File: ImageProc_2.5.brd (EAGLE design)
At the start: 49.8 x 23.2 mm, 117 parts, among them IC1 XC61GC3002HR-G, IC10 AT45DB642D-CNU, IC2 MIC5335-SPYMT, IC3 MIC5335-JGYMT, IC4 DSPIC33FJ128MC706A, IC5 AT86RF233-ZU, IC6 LTC6088, IC7 DRV8833RTY, IC8 DRV8833RTY, IC9 MPU-6000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

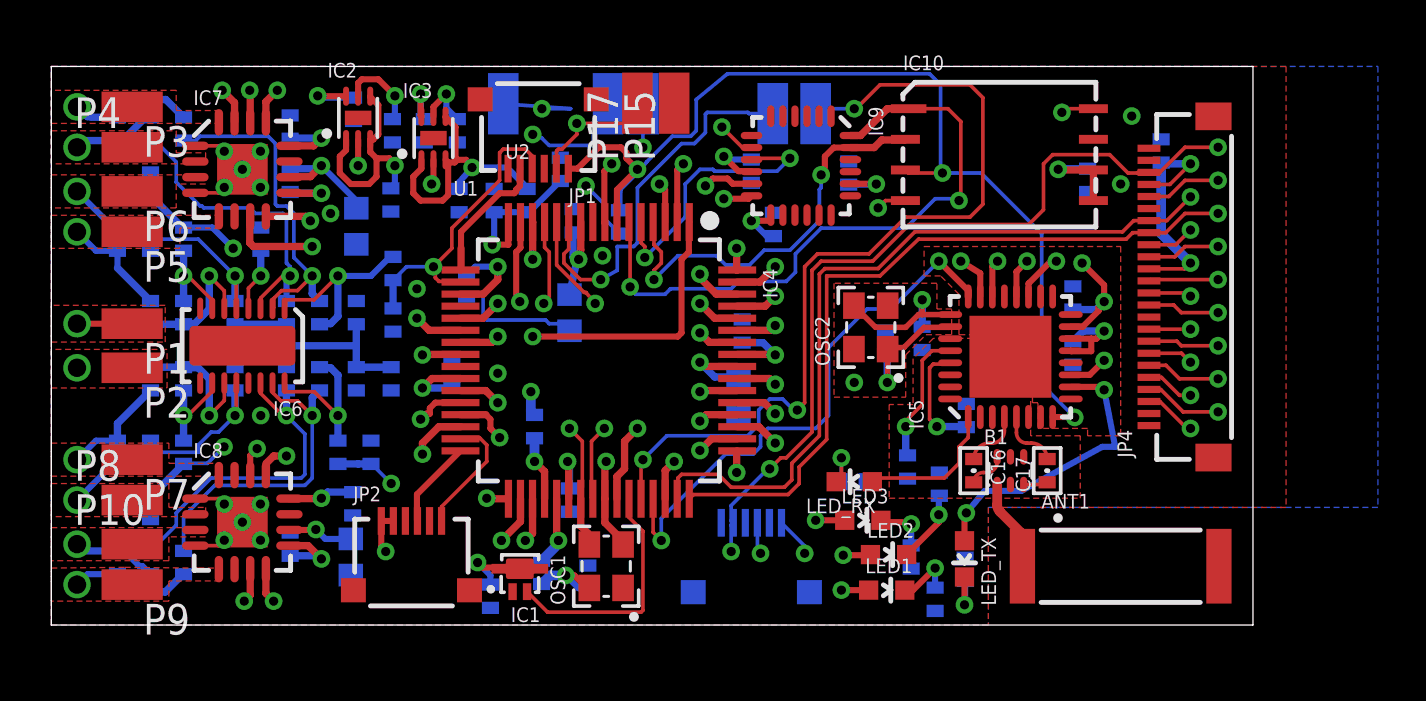
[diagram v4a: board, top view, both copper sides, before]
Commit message: Zero Airwires, fixed the restrict DRC errors.
Now proceeding to (hopefully final) DRC
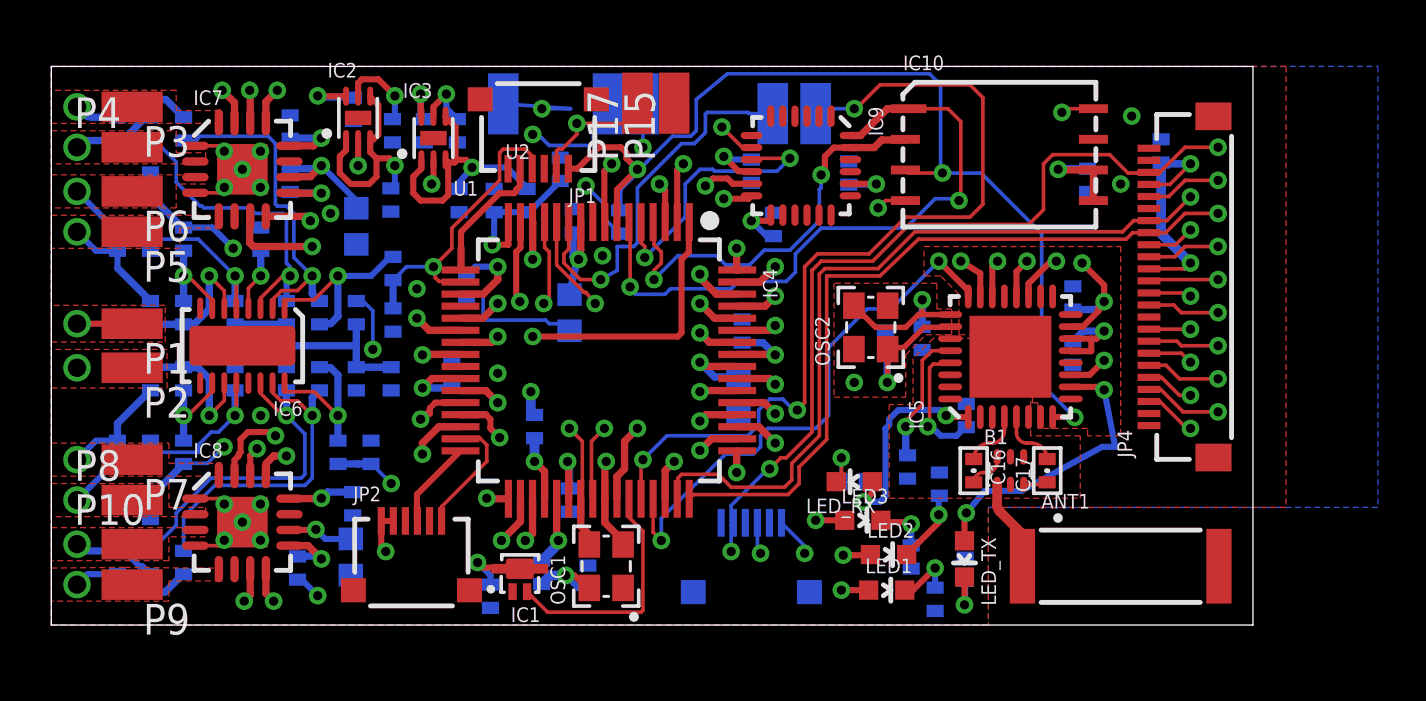
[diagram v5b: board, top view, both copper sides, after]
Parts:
- moved C34 1.04 mm to (10.2, 2.36), turned to 90 degrees
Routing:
- net V_BATT: track 37.6 -> 41.9 mm, vias 8 -> 10
- net N$13: track 5.99 -> 9.04 mm, vias 0 -> 2
- net 3.3V: track 61.2 -> 63.6 mm, vias 16 -> 17
- net N$3: track 4.73 -> 5.31 mm
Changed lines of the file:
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@@
 <grid distance="3" unitdist="mil" unit="mil" style="lines" multiple="1" display="yes" altdistance="1" altunitdist="mil" altunit="mil"/>
 <layers>
-<layer number="1" name="Top" color="4" fill="1" visible="no" active="yes"/>
+<layer number="1" name="Top" color="4" fill="1" visible="yes" active="yes"/>
 <layer number="2" name="Ground" color="2" fill="1" visible="no" active="yes"/>
 <layer number="3" name="Power" color="5" fill="1" visible="no" active="yes"/>
@@
 <layer number="14" name="Route14" color="1" fill="6" visible="no" active="no"/>
 <layer number="15" name="Route15" color="4" fill="6" visible="no" active="no"/>
-<layer number="16" name="Bottom" color="1" fill="1" visible="yes" active="yes"/>
+<layer number="16" name="Bottom" color="1" fill="1" visible="no" active="yes"/>
 <layer number="17" name="Pads" color="2" fill="1" visible="no" active="yes"/>
 <layer number="18" name="Vias" color="2" fill="1" visible="yes" active="yes"/>
-<layer number="19" name="Unrouted" color="6" fill="1" visible="yes" active="yes"/>
+<layer number="19" name="Unrouted" color="6" fill="1" visible="no" active="yes"/>
 <layer number="20" name="Dimension" color="15" fill="1" visible="no" active="yes"/>
 <layer number="21" name="tPlace" color="16" fill="1" visible="no" active="yes"/>
 <layer number="22" name="bPlace" color="14" fill="1" visible="no" active="yes"/>
 <layer number="23" name="tOrigins" color="15" fill="1" visible="no" active="yes"/>
-<layer number="24" name="bOrigins" color="15" fill="1" visible="no" active="yes"/>
+<layer number="24" name="bOrigins" color="15" fill="1" visible="yes" active="yes"/>
 <layer number="25" name="tNames" color="7" fill="1" visible="no" active="yes"/>
 <layer number="26" name="bNames" color="7" fill="1" visible="no" active="yes"/>
@@
 <layer number="39" name="tKeepout" color="4" fill="11" visible="no" active="yes"/>
 <layer number="40" name="bKeepout" color="1" fill="11" visible="no" active="yes"/>
-<layer number="41" name="tRestrict" color="4" fill="10" visible="no" active="yes"/>
-<layer number="42" name="bRestrict" color="1" fill="10" visible="no" active="yes"/>
+<layer number="41" name="tRestrict" color="4" fill="10" visible="yes" active="yes"/>
+<layer number="42" name="bRestrict" color="1" fill="10" visible="yes" active="yes"/>
 <layer number="43" name="vRestrict" color="2" fill="10" visible="no" active="yes"/>
 <layer number="44" name="Drills" color="7" fill="1" visible="no" active="yes"/>
@@
 <attribute name="TECHNOLOGY" value="CERAMIC" x="9.906" y="18.4404" size="1.778" layer="28" rot="MR270" display="off"/>
 </element>
-<element name="C34" library="biomimetic" package="0402-CAP" value="10nF" x="9.906" y="3.3528" locked="yes" rot="MR270">
-<attribute name="AUTHOR" value="Ryan Julian (ryanjulian@berkeley.edu)" x="9.906" y="3.3528" size="1.778" layer="28" rot="MR270" display="off"/>
-<attribute name="REVISION" value="1" x="9.906" y="3.3528" size="1.778" layer="28" rot="MR270" display="off"/>
-<attribute name="YEAR" value="2012" x="9.906" y="3.3528" size="1.778" layer="28" rot="MR270" display="off"/>
-<attribute name="DIELECTRIC" value="X7R" x="9.906" y="3.3528" size="1.778" layer="28" rot="MR270" display="off"/>
-<attribute name="TECHNOLOGY" value="CERAMIC" x="9.906" y="3.3528" size="1.778" layer="28" rot="MR270" display="off"/>
-<attribute name="VOLTAGE" value="16V" x="9.906" y="3.3528" size="1.778" layer="28" rot="MR270" display="off"/>
+<element name="C34" library="biomimetic" package="0402-CAP" value="10nF" x="10.2108" y="2.3622" rot="MR90">
+<attribute name="AUTHOR" value="Ryan Julian (ryanjulian@berkeley.edu)" x="10.2108" y="2.3622" size="1.778" layer="28" rot="MR90" display="off"/>
+<attribute name="REVISION" value="1" x="10.2108" y="2.3622" size="1.778" layer="28" rot="MR90" display="off"/>
+<attribute name="YEAR" value="2012" x="10.2108" y="2.3622" size="1.778" layer="28" rot="MR90" display="off"/>
+<attribute name="DIELECTRIC" value="X7R" x="10.2108" y="2.3622" size="1.778" layer="28" rot="MR90" display="off"/>
+<attribute name="TECHNOLOGY" value="CERAMIC" x="10.2108" y="2.3622" size="1.778" layer="28" rot="MR90" display="off"/>
+<attribute name="VOLTAGE" value="16V" x="10.2108" y="2.3622" size="1.778" layer="28" rot="MR90" display="off"/>
 </element>
 <element name="C24" library="biomimetic" package="0402-CAP" value="0.1uF" x="2.7432" y="20.574" rot="MR270">
@@
 <wire x1="30.2822" y1="4.2396" x2="31.242" y2="3.2798" width="0.1524" layer="16"/>
 <wire x1="31.242" y1="3.2798" x2="31.242" y2="2.9718" width="0.1524" layer="16"/>
-<wire x1="8.6868" y1="14.478" x2="12.6492" y2="13.4366" width="0" layer="19" extent="1-16"/>
+<via x="13.335" y="11.43" extent="1-16" drill="0.381"/>
+<wire x1="13.335" y1="11.43" x2="13.335" y2="13.0302" width="0.1524" layer="16"/>
+<wire x1="13.335" y1="13.0302" x2="12.9286" y2="13.4366" width="0.1524" layer="16"/>
+<wire x1="12.9286" y1="13.4366" x2="12.6492" y2="13.4366" width="0.1524" layer="16"/>
 </signal>
 <signal name="N$6">
@@
 <contactref element="IC5" pad="1"/>
 <wire x1="34.0494" y1="5.9436" x2="34.2018" y2="6.096" width="0.1524" layer="1"/>
-<wire x1="34.2018" y1="6.096" x2="37.0332" y2="6.096" width="0.1524" layer="1"/>
-<wire x1="37.0332" y1="6.096" x2="37.6428" y2="6.7056" width="0.1524" layer="1"/>
-<wire x1="37.6428" y1="6.7056" x2="37.6428" y2="7.3914" width="0.1524" layer="1"/>
-<wire x1="37.6428" y1="7.3914" x2="38.0264" y2="7.775" width="0.1524" layer="1"/>
-<wire x1="38.0264" y1="7.775" x2="38.0264" y2="8.6252" width="0.1524" layer="1"/>
+<via x="33.6804" y="5.1054" extent="1-16" drill="0.381"/>
+<wire x1="33.6804" y1="5.1054" x2="34.0494" y2="5.4744" width="0.254" layer="1"/>
+<wire x1="34.0494" y1="5.4744" x2="34.0494" y2="5.9436" width="0.254" layer="1"/>
+<via x="37.1094" y="8.6868" extent="1-16" drill="0.381"/>
+<wire x1="37.1094" y1="8.6868" x2="37.171" y2="8.6252" width="0.254" layer="1"/>
+<wire x1="37.171" y1="8.6252" x2="38.0264" y2="8.6252" width="0.254" layer="1"/>
+<wire x1="37.1094" y1="8.6868" x2="36.8808" y2="8.9154" width="0.254" layer="16"/>
+<wire x1="36.8808" y1="8.9154" x2="35.1282" y2="8.9154" width="0.254" layer="16"/>
+<wire x1="35.1282" y1="8.9154" x2="34.7472" y2="8.5344" width="0.254" layer="16"/>
+<wire x1="34.7472" y1="8.5344" x2="34.7472" y2="8.3058" width="0.254" layer="16"/>
+<wire x1="34.7472" y1="8.3058" x2="34.5948" y2="8.1534" width="0.254" layer="16"/>
+<wire x1="34.5948" y1="8.1534" x2="34.5948" y2="5.334" width="0.254" layer="16"/>
+<wire x1="34.5948" y1="5.334" x2="34.3662" y2="5.1054" width="0.254" layer="16"/>
+<wire x1="34.3662" y1="5.1054" x2="33.6804" y2="5.1054" width="0.254" layer="16"/>
 </signal>
 <signal name="N$14">
@@
 <wire x1="9.8748" y1="3.2922" x2="10.6524" y2="3.2922" width="0.3048" layer="1"/>
 <wire x1="10.6524" y1="3.2922" x2="11.2014" y2="2.7432" width="0.3048" layer="1"/>
-<wire x1="9.906" y1="2.8702" x2="11.0744" y2="2.8702" width="0.3048" layer="16"/>
+<wire x1="10.2108" y1="2.8448" x2="11.0744" y2="2.8702" width="0.3048" layer="16"/>
 <wire x1="11.0744" y1="2.8702" x2="11.2014" y2="2.7432" width="0.3048" layer="16"/>
 </signal>
@@
 <wire x1="17.4498" y1="18.9738" x2="16.9164" y2="18.3642" width="0.254" layer="16"/>
 <wire x1="16.9164" y1="18.3642" x2="16.9164" y2="18.0848" width="0.254" layer="16"/>
-<wire x1="9.8748" y1="3.9422" x2="9.906" y2="3.8354" width="0" layer="19" extent="1-16"/>
-<wire x1="7.5998" y1="6.2172" x2="9.8748" y2="3.9422" width="0" layer="19" extent="1-1"/>
+<via x="9.2964" y="7.8486" extent="1-16" drill="0.381"/>
+<wire x1="9.2964" y1="7.8486" x2="9.144" y2="8.001" width="0.254" layer="1"/>
+<wire x1="9.144" y1="8.001" x2="8.1534" y2="8.001" width="0.254" layer="1"/>
+<wire x1="8.1534" y1="8.001" x2="7.8486" y2="7.6962" width="0.254" layer="1"/>
+<wire x1="7.8486" y1="7.6962" x2="7.8486" y2="7.1628" width="0.254" layer="1"/>
+<wire x1="7.8486" y1="7.1628" x2="7.7724" y2="7.0866" width="0.254" layer="1"/>
+<wire x1="7.7724" y1="7.0866" x2="7.7724" y2="7.0104" width="0.254" layer="1"/>
+<wire x1="7.7724" y1="7.0104" x2="7.5998" y2="6.8378" width="0.254" layer="1"/>
+<wire x1="7.5998" y1="6.8378" x2="7.5998" y2="6.2172" width="0.254" layer="1"/>
+<via x="11.049" y="1.2192" extent="1-16" drill="0.381"/>
+<wire x1="11.049" y1="1.2192" x2="10.3886" y2="1.8796" width="0.254" layer="16"/>
+<wire x1="10.3886" y1="1.8796" x2="10.2108" y2="1.8796" width="0.254" layer="16"/>
 </signal>
 <signal name="N$10">
@@
 <contactref element="IC5" pad="29"/>
 <contactref element="C20" pad="2"/>
-<via x="36.7284" y="8.2296" extent="1-16" drill="0.381"/>
+<via x="36.3474" y="8.2296" extent="1-16" drill="0.381"/>
 <wire x1="37.2216" y1="10.8204" x2="37.2764" y2="10.8752" width="0.1524" layer="1"/>
 <wire x1="37.2216" y1="10.8204" x2="36.576" y2="10.8204" width="0.1524" layer="1"/>
 <wire x1="36.576" y1="10.8204" x2="36.4236" y2="10.668" width="0.1524" layer="1"/>
 <wire x1="36.4236" y1="10.668" x2="36.4236" y2="8.5344" width="0.1524" layer="1"/>
-<wire x1="36.4236" y1="8.5344" x2="36.7284" y2="8.2296" width="0.1524" layer="1"/>
+<wire x1="36.4236" y1="8.5344" x2="36.3474" y2="8.2296" width="0.1524" layer="1"/>
 <wire x1="37.9476" y1="8.2042" x2="37.9222" y2="8.2296" width="0.3048" layer="16"/>
-<wire x1="37.9222" y1="8.2296" x2="36.7284" y2="8.2296" width="0.3048" layer="16"/>
+<wire x1="37.9222" y1="8.2296" x2="37.5412" y2="7.8486" width="0.254" layer="16"/>
+<wire x1="37.5412" y1="7.8486" x2="36.8808" y2="7.8486" width="0.254" layer="16"/>
+<wire x1="36.8808" y1="7.8486" x2="36.4998" y2="8.2296" width="0.254" layer="16"/>
+<wire x1="36.4998" y1="8.2296" x2="36.3474" y2="8.2296" width="0.254" layer="16"/>
 </signal>
 <signal name="N$1">

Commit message: 0 Airwires, 0 non-ignored DRC Errors.
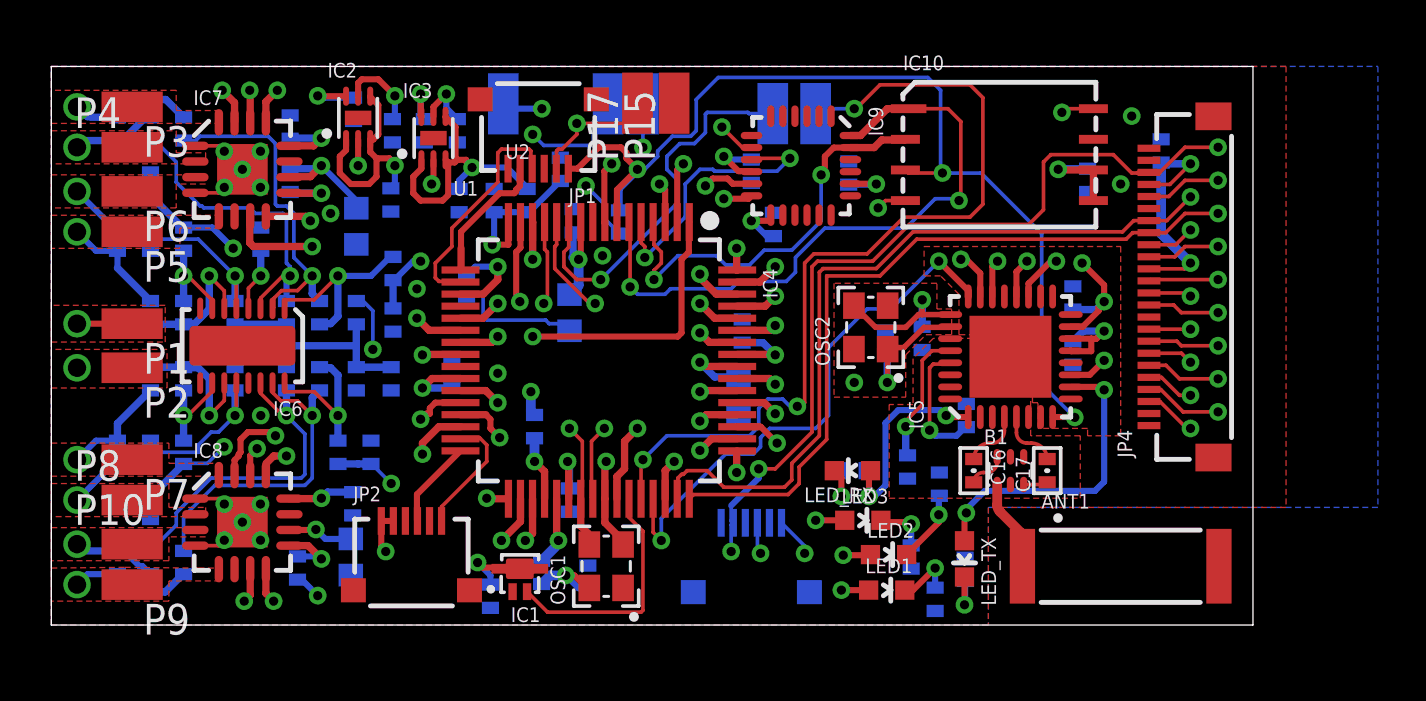
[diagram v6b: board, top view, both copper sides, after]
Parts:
- moved LED_RX 0.46 mm to (33.2, 6.40)
- moved R7 0.46 mm to (33.2, 6.40)
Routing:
- net MOTOR_C_IN2: track 41.7 -> 48.6 mm
- net AN3/INDX/RB3: track 21.2 -> 15.9 mm
- net AN1/RB1: track 20.2 -> 15.6 mm
- net 3.3V: track 63.6 -> 64.9 mm
- net MOTOR_C_IN1: track 35.2 -> 36.2 mm
- net N$13: track 9.04 -> 8.33 mm
- net N$14: track 12.1 -> 12.8 mm
- net !SS1: track 27.9 -> 28.5 mm
